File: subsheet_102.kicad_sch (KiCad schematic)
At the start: 32 parts

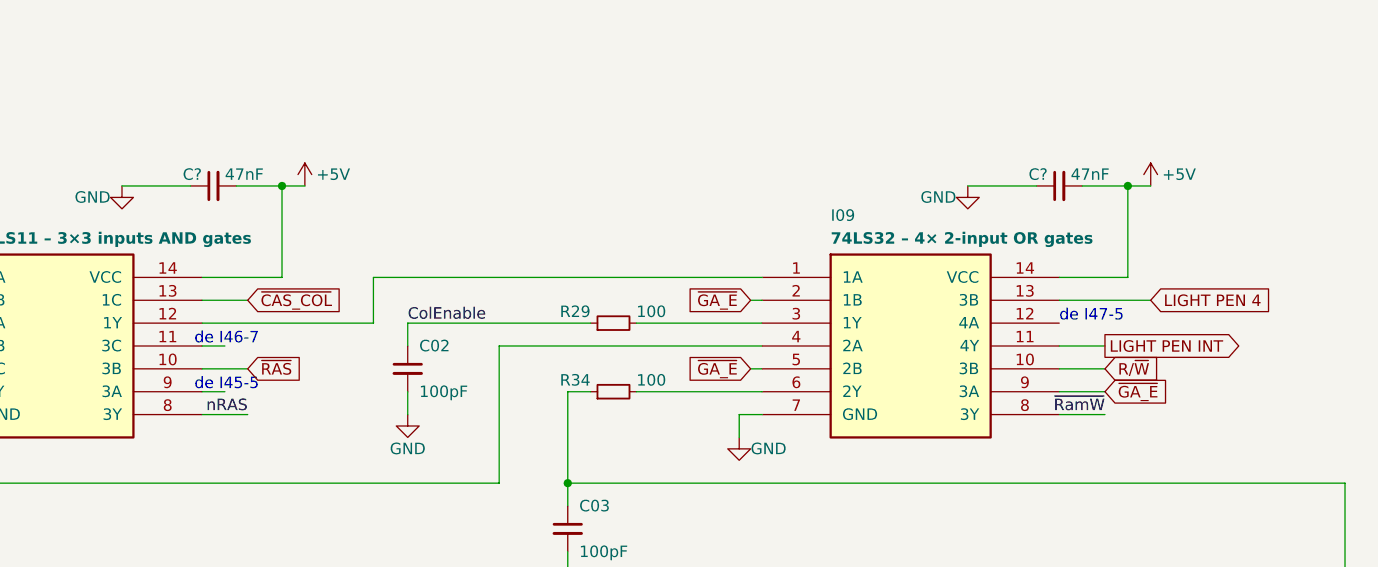
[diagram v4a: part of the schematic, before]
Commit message: rename GA_E/GA_Q/~{GA_E} into E/Q/~{E}
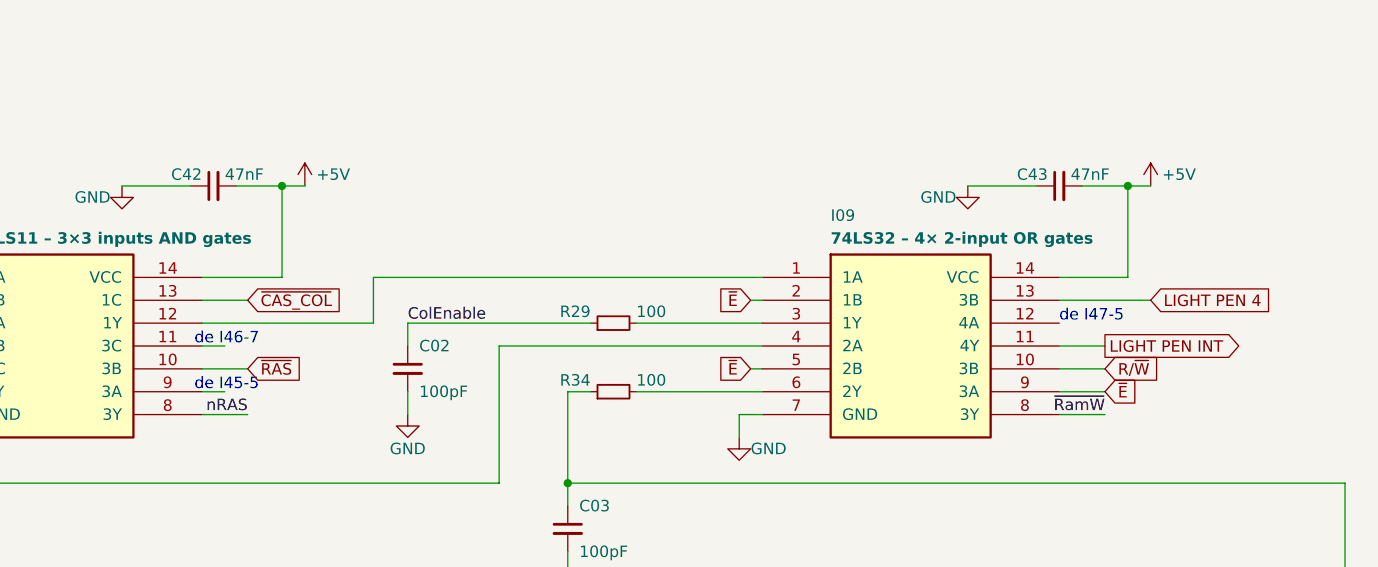
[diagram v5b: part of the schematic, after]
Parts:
- gave numbers to parts that had none: 2
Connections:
- net ~{GA_E} renamed ~{E}
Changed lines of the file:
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@@
     )
   )
-  (global_label "~{GA_E}" (shape input) (at 128.27 76.2 180) (fields_autoplaced)
+  (global_label "~{E}" (shape input) (at 128.27 76.2 180) (fields_autoplaced)
     (effects (font (size 1.27 1.27)) (justify right))
-    (property "Intersheet References" "${INTERSHEET_REFS}" (id 0) (at 121.3817 76.1206 0)
+    (property "Intersheet References" "${INTERSHEET_REFS}" (id 0) (at 124.7079 76.1206 0)
       (effects (font (size 1.27 1.27)) (justify right) hide)
     )
@@
     )
   )
-  (global_label "~{GA_E}" (shape input) (at 167.64 78.74 0) (fields_autoplaced)
+  (global_label "~{E}" (shape input) (at 167.64 78.74 0) (fields_autoplaced)
     (effects (font (size 1.27 1.27)) (justify left))
-    (property "Intersheet References" "${INTERSHEET_REFS}" (id 0) (at 174.5283 78.8194 0)
+    (property "Intersheet References" "${INTERSHEET_REFS}" (id 0) (at 171.2021 78.6606 0)
       (effects (font (size 1.27 1.27)) (justify left) hide)
     )
@@
     )
   )
-  (global_label "~{GA_E}" (shape input) (at 128.27 68.58 180) (fields_autoplaced)
+  (global_label "~{E}" (shape input) (at 128.27 68.58 180) (fields_autoplaced)
     (effects (font (size 1.27 1.27)) (justify right))
-    (property "Intersheet References" "${INTERSHEET_REFS}" (id 0) (at 121.3817 68.5006 0)
+    (property "Intersheet References" "${INTERSHEET_REFS}" (id 0) (at 124.7079 68.5006 0)
       (effects (font (size 1.27 1.27)) (justify right) hide)
     )
@@
   (symbol (lib_id "Device:C_Small") (at 68.58 55.88 90) (unit 1)
     (in_bom yes) (on_board yes)
-    (property "Reference" "C?" (id 0) (at 67.31 54.61 90)
+    (property "Reference" "C42" (id 0) (at 67.31 54.61 90)
       (effects (font (size 1.27 1.27)) (justify left))
     )
@@
   (symbol (lib_id "Device:C_Small") (at 162.56 55.88 90) (unit 1)
     (in_bom yes) (on_board yes)
-    (property "Reference" "C?" (id 0) (at 161.29 54.61 90)
-      (effects (font (size 1.27 1.27)) (justify left))
-    )
+    (property "Reference" "C43" (id 0) (at 161.29 54.61 90)
+      (effects (font (size 1.27 1.27)) (justify left))
+    )

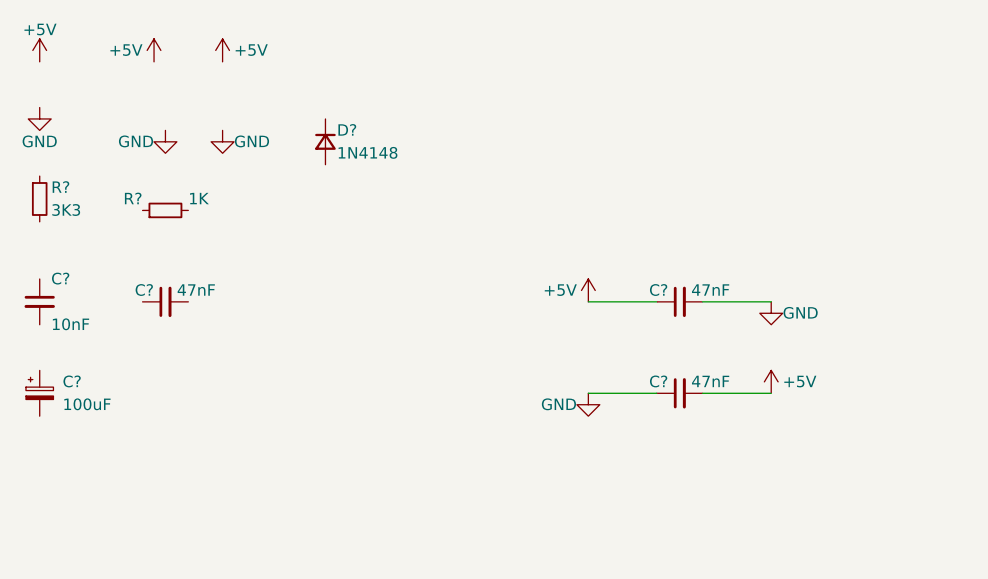
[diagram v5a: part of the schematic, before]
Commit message: commence le circuit d'alimentation
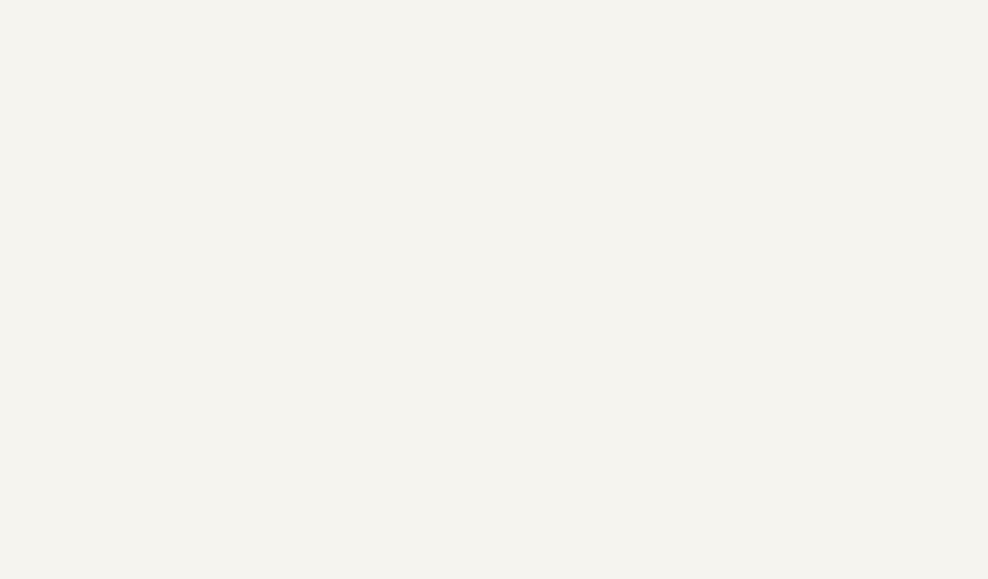
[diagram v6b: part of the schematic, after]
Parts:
- removed C? (x3): 47nF, symbol Device:C_Small
- removed C?: 100uF, symbol Device:C_Polarized_Small
- removed C?: 10nF, symbol Device:C_Small
- removed D?: 1N4148, symbol Device:D_Small
- removed R?: 1K, symbol Device:R_Small
- removed R?: 3K3, symbol Device:R_Small

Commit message: remise au propre
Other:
- title: Conversion du Thomson MO5 — Unité centrale -> Conversion du Thomson MO5 — Unité centrale v1
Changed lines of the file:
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@@
   (paper "A4" portrait)
   (title_block
-    (title "Conversion du Thomson MO5 — Unité centrale")
-    (date "2023-05-12")
+    (title "Conversion du Thomson MO5 — Unité centrale v1")
+    (date "2023-05-14")
     (rev "DRAFT")
     (comment 1 "http://github.com/sporniket/kicad-conversions--thomson-mo5--v1")
-    (comment 2 "Dépôt d'origine : ")
+    (comment 3 "Gate Array Motorola MCA 1300 ALS")
     (comment 4 "Reference : POP5001 501994-01")
   )

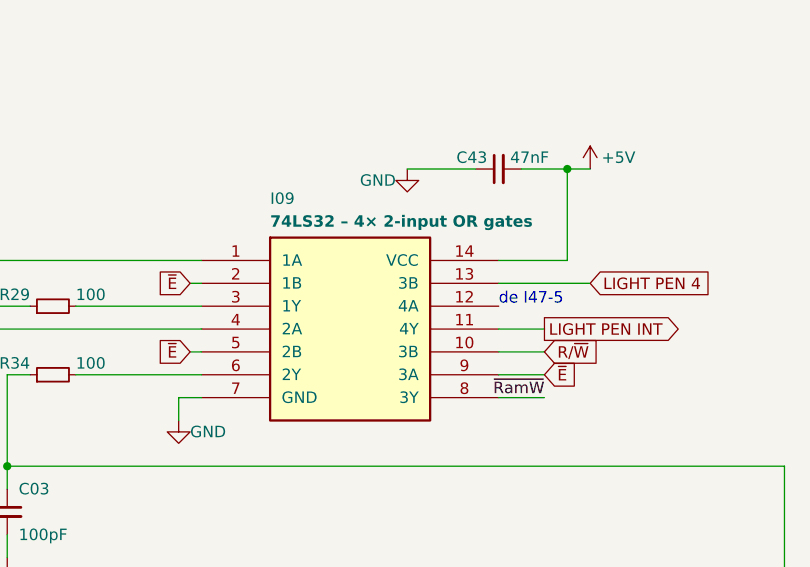
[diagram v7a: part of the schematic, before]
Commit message: fix 74x32 symbol ; better visualization from light pen pin 4 to light pen interrupt signal
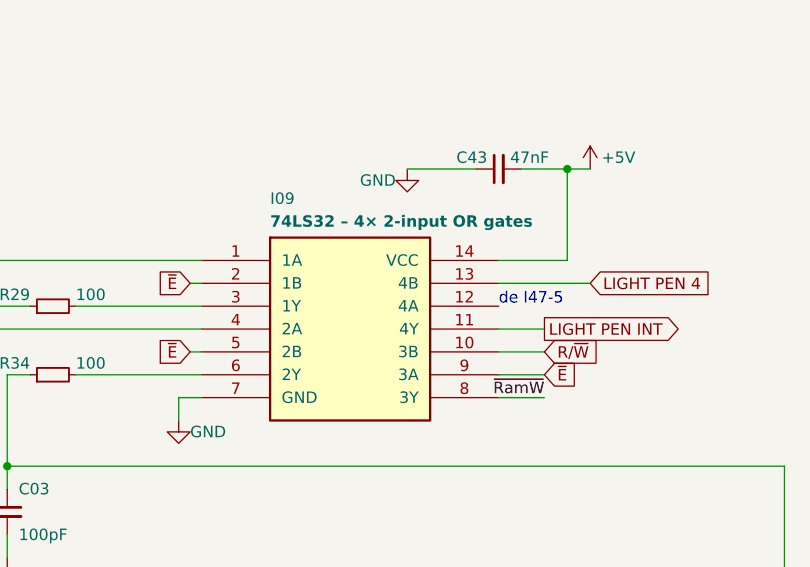
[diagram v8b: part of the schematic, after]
